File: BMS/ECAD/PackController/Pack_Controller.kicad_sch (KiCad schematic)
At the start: 0 parts

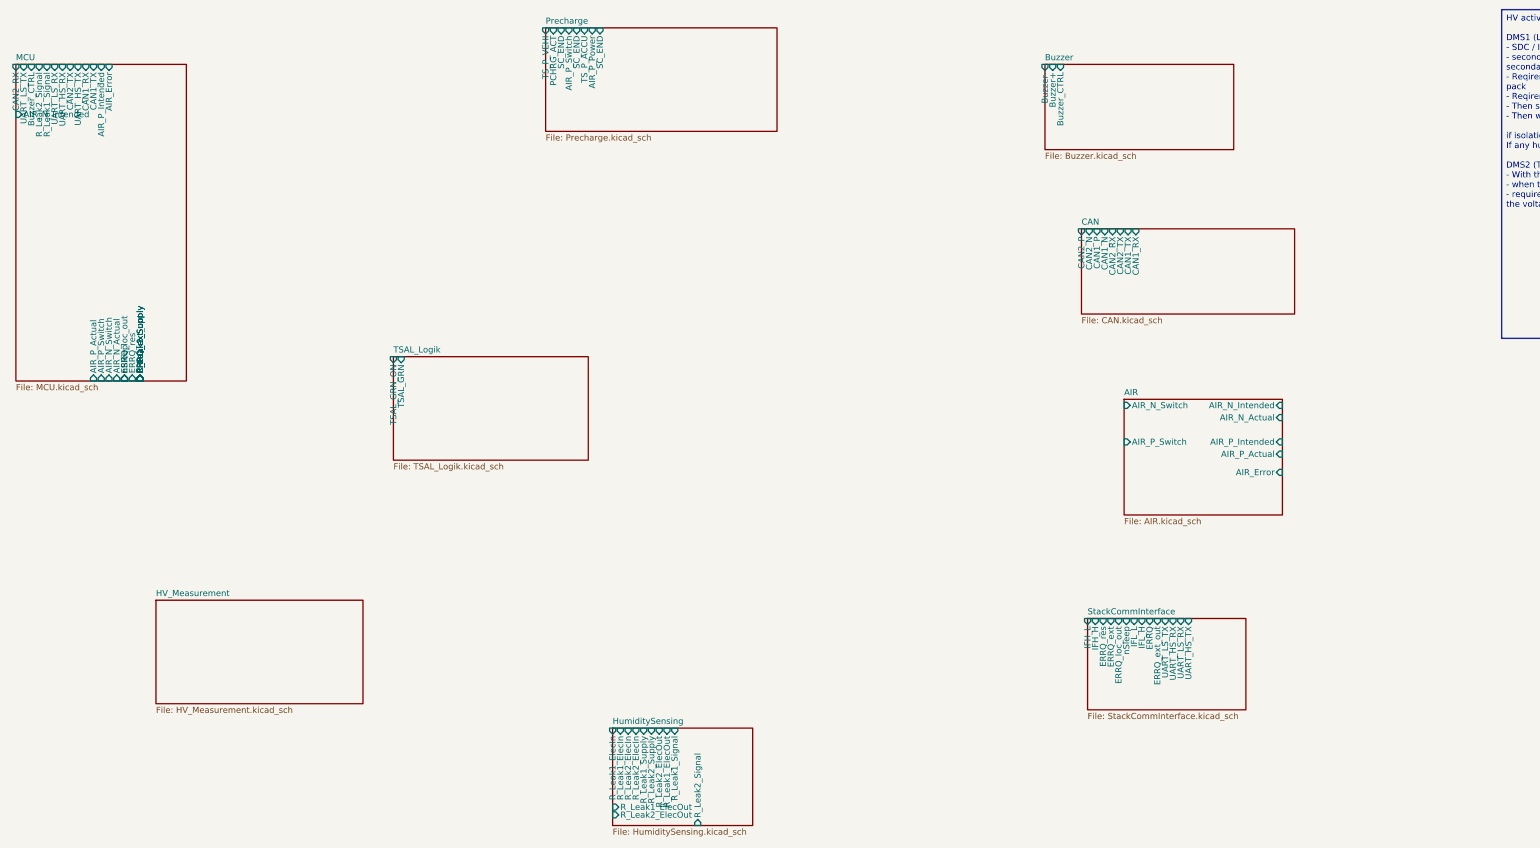
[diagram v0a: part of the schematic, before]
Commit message: implement HV measurement
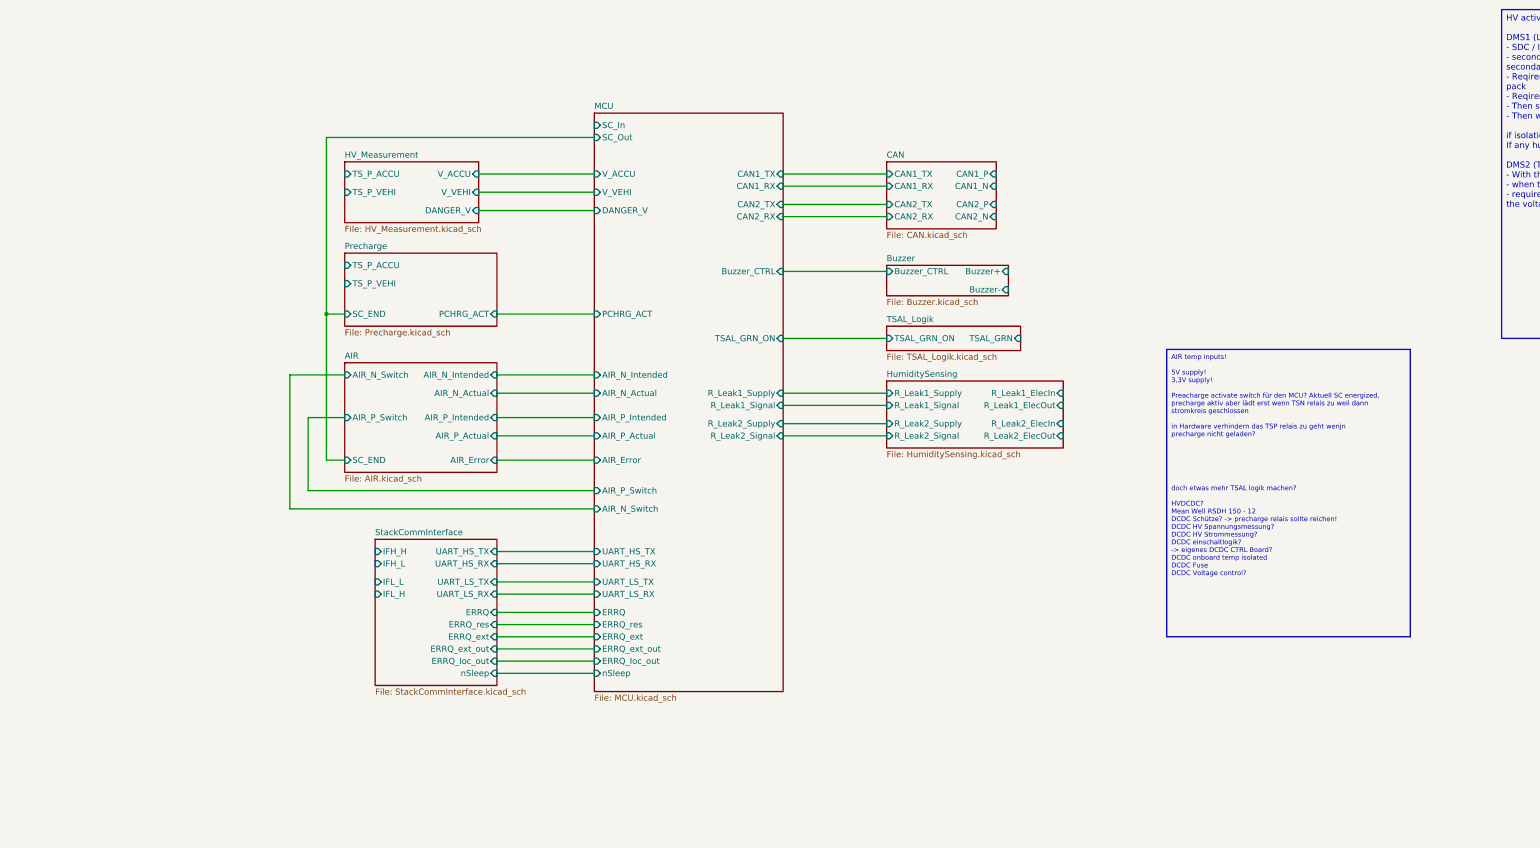
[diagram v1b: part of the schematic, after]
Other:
- sheet AIR ports: added SC_END; removed none
- sheet HV_Measurement ports: added DANGER_V, TS_P_ACCU, TS_P_VEHI, V_ACCU, V_VEHI; removed none
- sheet MCU ports: added DANGER_V, PCHRG_ACT, SC_In, SC_Out, TSAL_GRN_ON, V_ACCU, V_VEHI; removed none
- sheet Precharge ports: added none; removed AIR_P_Power, AIR_P_Switch

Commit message: schematic finished, review tbd
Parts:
- added BUZZ, ISOUART_H, ISOUART_L: Conn_01x02, symbol Connector_Generic:Conn_01x02
- added J2: Conn_01x10, symbol Connector_Generic:Conn_01x10
- added J_HV_ACCU, J_HV_VEHI: Conn_01x04, symbol Connector_Generic:Conn_01x04
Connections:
- net Buzzer/Buzzer+: now also BUZZ.1 (Pin_1)
- net Buzzer/Buzzer-: now also BUZZ.2 (Pin_2)
- net HV_Measurement/TS_P_ACCU: now also J_HV_ACCU.1 (Pin_1)
- net HV_Measurement/TS_P_VEHI: now also J_HV_VEHI.1 (Pin_1)
- net MCU/SC_In: now also J2.1 (Pin_1)
- net StackCommInterface/IFH_H: now also ISOUART_H.1 (Pin_1)
- net StackCommInterface/IFH_L: now also ISOUART_H.2 (Pin_2)
- net StackCommInterface/IFL_H: now also ISOUART_L.1 (Pin_1)
- net StackCommInterface/IFL_L: now also ISOUART_L.2 (Pin_2)
- net TSAL_Logik/TSAL_GRN: now also J2.10 (Pin_10)
- new net +BATT: J2.2 (Pin_2), J2.3 (Pin_3)
- new net CAN1/CAN_N: J2.7 (Pin_7)
- new net CAN1/CAN_P: J2.6 (Pin_6)
- new net CAN2/CAN_N: J2.9 (Pin_9)
- new net CAN2/CAN_P: J2.8 (Pin_8)
- new net GND: J2.4 (Pin_4), J2.5 (Pin_5)
- new net HV_Measurement/TS_N_ACCU: J_HV_ACCU.4 (Pin_4)
- new net HV_Measurement/TS_N_VEHI: J_HV_VEHI.4 (Pin_4)
- no-connect marks 0 -> 4
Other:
- sheet CAN renamed CAN1
- added sheet CAN2 (CAN.kicad_sch)
- added sheet Supply (Supply.kicad_sch)
- added sheet TempMeas (TempMeas.kicad_sch)
- sheet CAN1 ports: added CAN_N, CAN_P, CAN_RX, CAN_TX; removed CAN1_N, CAN1_P, CAN1_RX, CAN1_TX, CAN2_N, CAN2_P, CAN2_RX, CAN2_TX
- sheet HV_Measurement ports: added TS_N_ACCU, TS_N_VEHI; removed none
- sheet HumiditySensing ports: added R_Leak_Sig1, R_Leak_Sig2, R_Leak_Supply1, R_Leak_Supply2; removed R_Leak1_ElecIn, R_Leak1_ElecOut, R_Leak1_Signal, R_Leak1_Supply, R_Leak2_ElecIn, R_Leak2_ElecOut, R_Leak2_Signal, R_Leak2_Supply
- sheet MCU ports: added NTC1_Sig, NTC2_Sig, NTC3_Sig, PCHRG_SWITCH; removed none
- sheet Precharge ports: added PCHRG_ACTUAL, PCHRG_SWITCH; removed PCHRG_ACT

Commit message: close to finish BMS master, only some footprints needed
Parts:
- removed J_HV_VEHI: Conn_01x04, symbol Connector_Generic:Conn_01x04
- added HV_VEHI: 436500415, Connector_PinSocket_1.00mm:PinSocket_1x04_P1.00mm_Vertical, symbol Connector_Generic:Conn_01x04
- HV_ACCU: renamed from J_HV_ACCU; value Conn_01x04 -> 436500415; footprint (none) -> Connector_PinSocket_1.00mm:PinSocket_1x04_P1.00mm_Vertical
- ISOUART_H, ISOUART_L: value Conn_01x02 -> 436500227; footprint (none) -> Connector_PinSocket_1.00mm:PinSocket_1x02_P1.00mm_Vertical
- renumbered BUZZ to BUZZ101, J2 to J101
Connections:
- net HV_Measurement/TS_N_VEHI: now also HV_VEHI.4 (Pin_4)
- net HV_Measurement/TS_P_VEHI: now also HV_VEHI.1 (Pin_1)
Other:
- sheet AIR ports: added DANGER_V, PRCHG_DONE; removed none
- sheet HV_Measurement ports: added nDANGER_V; removed none
- sheet MCU ports: added PCHRG_ACTUAL, nDANGER_V, nPRCHG_DONE; removed DANGER_V, PCHRG_ACT
- sheet Precharge ports: added PRCHG_DONE, V_ACCU, V_VEHI, nPRCHG_DONE; removed none
